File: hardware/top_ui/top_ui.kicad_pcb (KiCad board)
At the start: 2 copper layers, 52 x 52 mm, 26 parts, among them J1 USB-C, J2 J_STK_A, J3 J_STK_B, J5 ST77916 QSPI, J6 Stern, J7 Radar, Q1 BC847, Q2 P-FET 20V 1A, SW1A BTN1, SW1B BTN1, SW2A BTN2, SW2B BTN2, SW3A BTN3, SW3B BTN3, SW4A BTN4, SW4B BTN4, U1 USBLC6-2SC6, U2 SHT40-AD1B

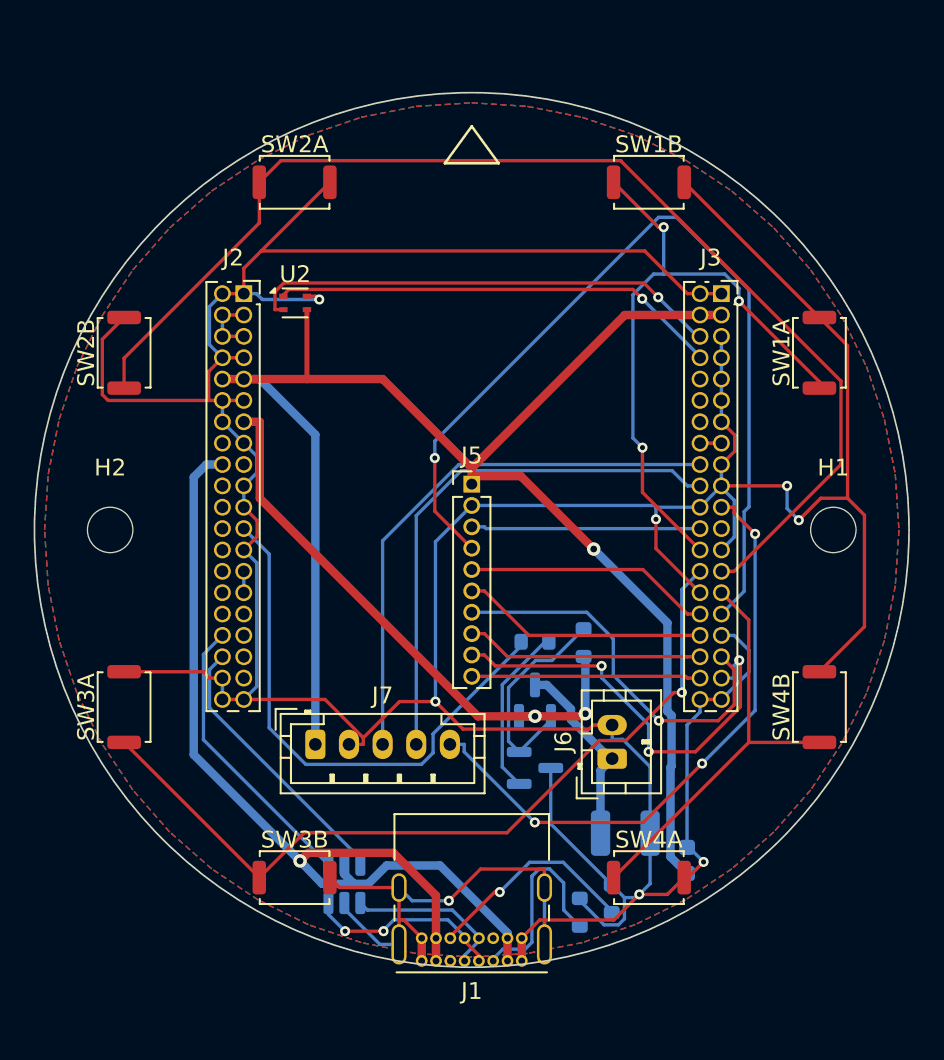
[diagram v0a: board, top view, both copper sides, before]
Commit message: Reed-Kontakte, Haubenkontakt, Klinkenbuchse, ToF statt Radar
Funktional neu
--------------
- Zwei Reed-Eingaenge fuer Fensterkontakte auf den einzigen noch freien
  Expanderpins P6/P7. 10k Pullup, 1k Serie, 100n und TVS je Kanal; bei
  geschlossenem Kontakt liegen 0,3 V am PCF8574, sicher unter VIL.
- Meldekontakt zur Dunstabzugshaube ueber PhotoMOS AQY282GS statt Relais:
  potentialfrei, 60 V / 0,8 A, kein Spulenstrom, keine Bauhoehe im 9-mm-
  Stapelspalt. NUR SELV - bei 230 V gehoert das Schaltglied nicht in die Dose.
- Weihnachtsstern jetzt gesteckt: Klinkenbuchse im oberen Steg der
  Frontplatte, PTC 0,2 A direkt an der Buchse gegen den Kurzschluss beim
  Stecken, Bulk vor die Sicherung gelegt.
- Radar durch VL53L1X (ToF) ersetzt. Hinter dieser Frontplatte hat kein
  20-mm-Radarmodul freie Sicht; der ToF passt als 4,9 x 2,5 mm grosser Chip
  in den Steg. Er misst Entfernung statt Empfindlichkeit - Schwelle exakt
  1 m - und deckt in der Fensterlaibung zugleich den Durchstieg ab.
  Netze umbenannt: RADAR_INT -> PRESENCE_INT, UART_RADAR_* -> UART_AUX_*.
  J7 bleibt unbestueckt als Reserve, damit das Stackpinout unberuehrt bleibt.

Frontplatte
-----------
Oberer Steg 9 -> 17 mm, damit Klinkenbuchse und ToF-Fenster nebeneinander
passen; Sicheln dadurch ~70 -> ~45 Grad, Stoesselwinkel 18 -> 12 Grad.
ToF-Kanal konisch (4,5 vorn, 3,0 hinten) fuer den Sichtkegel. Kabelausgang
Ø4,5 entfaellt. Selbsttests bestanden, STEP/STL neu erzeugt.

KiCad 10
--------
Die Generatoren liefen nur gegen KiCad-9-Bibliotheken. Migriert:
- Symbol- und Footprintpfad werden gefunden (Linux, macOS, Umgebungsvariable)
- PCF8574 -> PCF8574T (pinkompatibel, als Alias)
- Q_NMOS_GDS/Q_PMOS_GSD/Q_NPN_BCE liegen jetzt als hardware/lib/
  SwitchStack.kicad_sym im Projekt. KiCad 10 nummeriert die Stockvarianten
  mit G/D/S bzw. B/C/E - ein Alias haette die Anschluesse still vertauscht.
- USB-C-Schirm heisst SH statt S1, Zonen-API SetDoNotAllowZoneFills,
  DRC laeuft ueber kicad-cli statt WriteDRCRepo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
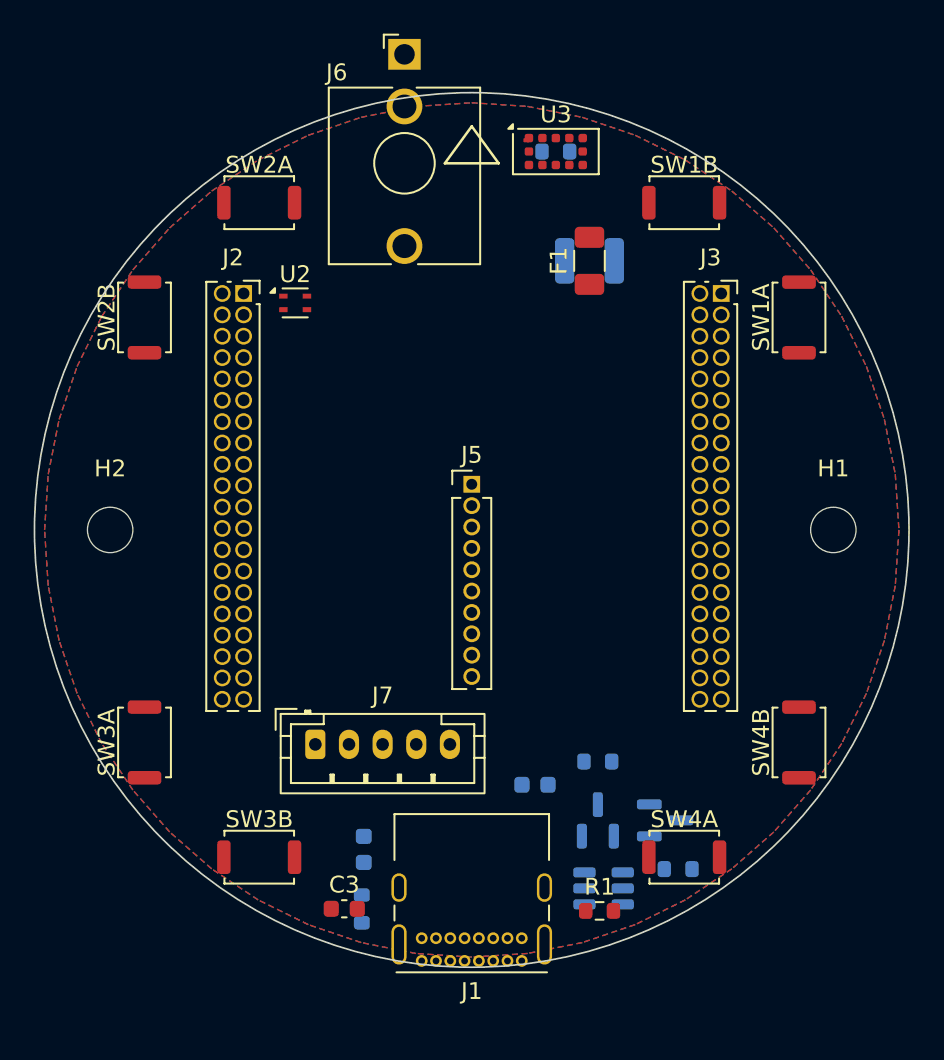
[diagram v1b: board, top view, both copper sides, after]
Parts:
- added C3: 100n, C_0603_1608Metric, F.Cu at (-7.58, 22.5)
- added C4: 4u7, C_0603_1608Metric, B.Cu at (-6.42, 19.0)
- added F1: 0,2 A PTC, Fuse_1206_3216Metric, F.Cu at (7.00, -16.0)
- added R5: 10k, R_0603_1608Metric, B.Cu at (5.00, -22.5)
- added U3: VL53L1X, ST_VL53L1x, F.Cu at (5.00, -22.5)
- J6: value Stern -> Stern Klinke; footprint JST_PH_B2B-PH-K_1x02_P2.00mm_Vertical -> Jack_3.5mm_QingPu_WQP-PJ398SM_Vertical_CircularHoles
- J7: value Radar -> Reserve UART
- R1: moved to F.Cu
- moved J6 43.7 mm to (-4.00, -28.3), turned to 0 degrees
- moved C2 34.1 mm to (7.00, -16.0)
- moved U1 15.4 mm to (7.84, 21.3), turned to 0 degrees
- moved R2 14.9 mm to (-6.54, 22.5)
- moved R4 14.6 mm to (12.3, 20.2), turned to 0 degrees
- moved Q2 10.5 mm to (11.5, 17.3), turned to 0 degrees
- moved C1 10.1 mm to (3.76, 15.2), turned to 0 degrees
- moved R3 8.04 mm to (7.50, 13.8)
- moved Q1 4.87 mm to (7.50, 17.3), turned to 90 degrees
- moved SW1A 2.43 mm to (19.5, -12.6)
- moved SW1B 2.43 mm to (12.6, -19.5)
- moved SW2A 2.43 mm to (-12.6, -19.5)
- moved SW2B 2.43 mm to (-19.5, -12.6)
- moved SW3A 2.43 mm to (-19.5, 12.6)
- moved SW3B 2.43 mm to (-12.6, 19.5)
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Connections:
- net RADAR_INT renamed PRESENCE_INT
- net UART_RADAR_RX renamed UART_AUX_RX
- net UART_RADAR_TX renamed UART_AUX_TX
- C2 pad 1: STAR_OUT -> STAR_SW
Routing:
- net PGND: track 302.5 -> 0.00 mm, vias 8 -> 0
- net 3V3_SYS: track 95.4 -> 0.00 mm, vias 1 -> 0
- net BTN2: track 70.8 -> 0.00 mm
- net USB_VBUS: track 58.7 -> 0.00 mm, vias 1 -> 0
- net QSPI_D0: track 53.2 -> 0.00 mm, vias 1 -> 0
- net BTN3: track 48.7 -> 0.00 mm, vias 1 -> 0
- net BTN1: track 38.8 -> 0.00 mm, vias 3 -> 0
- net PRESENCE_INT: track 36.4 -> 0.00 mm, vias 3 -> 0
- net 6V2_STAR_F: track 34.7 -> 0.00 mm, vias 2 -> 0
- net UART_AUX_TX: track 32.9 -> 0.00 mm
- net STAR_EN: track 32.2 -> 0.00 mm
- net UART_AUX_RX: track 32.0 -> 0.00 mm
- net I2C_SCL: track 28.4 -> 0.00 mm, vias 1 -> 0
- net I2C_SDA: track 26.7 -> 0.00 mm, vias 1 -> 0
- net DISP_RST: track 25.5 -> 0.00 mm, vias 3 -> 0
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
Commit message: Klinke nach 6 Uhr, ToF bleibt 12 Uhr - USB-C weicht nach oben aus
Beide Durchbrueche der Frontplatte sassen im oberen Steg. Der ToF gehoert
dorthin - er soll nach vorn und in die Fensteroeffnung schauen, nicht auf die
Fensterbank. Der Steckplatz gehoert nach unten, sonst haengt das Sternkabel
quer ueber der Anzeige.

Frontplatte
-----------
jack_x/jack_y von (-4,0 / +22,5) auf (0 / -22,5). Die Stegbreite bleibt: das
Ringskizze schneidet beide Rechtecke symmetrisch, alle vier Stege sind ohnehin
17 mm breit. Der Selbsttest pruefte fest verdrahtet den 90-Grad-Steg auf zwei
Durchbrueche; er sortiert die Loecher jetzt selbst nach Steg und prueft beide.
Materialbahnen: oben 11,25 und 1,25 mm, unten 5,70 und 5,70 mm. Selbsttest
BESTANDEN, STEP/STL neu erzeugt.

Top-Layout
----------
Die Klinke stand auf 6 Uhr im Weg - dort sass die USB-C-Buchse. Neue Ordnung:

  12 Uhr   ToF bei x=+5, USB-C links daneben (Mitte x=-3,875)
   6 Uhr   Klinkenbuchse mittig
   innen   J7 (Reserve-UART, DNP) nach rechts neben den Displayanschluss

Zur USB-C-Lage: Das Fenster zwischen dem ToF und dem Taster auf 123 Grad ist
knapp 12 mm breit. Tangential gedreht waechst die BBOX des Verbinders auf
12,2 mm - passt nicht. Achsparallel sind es 8,95 mm, es bleiben je 1,5 mm Luft.
Das Steckgesicht liegt dabei leicht innerhalb der Kontur; der Stecker ragt ueber
die 1 mm duenne Platine hinweg, das kostet nichts, waehrend Kupfer ueber der
Kante an die Dosenwand stiesse.

J7 musste weichen und findet automatisch keinen Platz: Als THT-Teil braucht er
beide Seiten frei, und die Vorderseite innerhalb r21 gehoert dem Displaymodul.
Deshalb wieder fest platziert, kurz zu J3, aus dem sein UART kommt.

Ergebnis: Platzierung kollisionsfrei, Randabstandsverletzungen 11 -> 1. Die
verbliebene ist der Platzhalter-Footprint der Klinke (Punkt 30): 14,4 mm lang
mit dem Bund in der Mitte, bei r = 22,5 steht das hintere Ende 3,3 mm ueber die
Kante. Punkt 30 nennt jetzt das Zielmass - das reale 2,5-mm-Teil muss in einen
Ring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
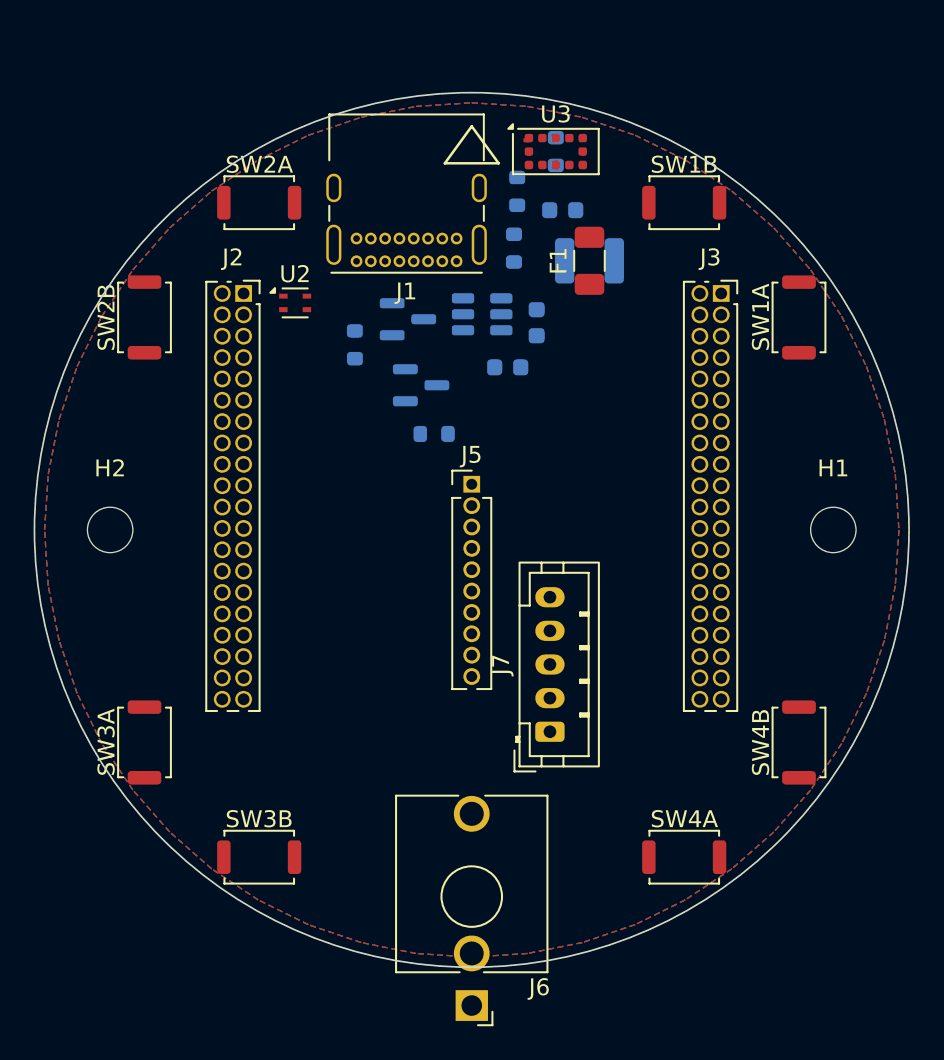
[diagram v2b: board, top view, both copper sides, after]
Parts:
- C3, R1: moved to B.Cu
- moved J6 56.7 mm to (0.00, 28.3), turned to 180 degrees
- moved R2 43.7 mm to (2.70, -20.1)
- moved J1 41.8 mm to (-0.90, -16.0)
- moved C4 39.8 mm to (5.41, -19.0), turned to 0 degrees
- moved R1 39.7 mm to (2.51, -16.8), turned to 90 degrees
- moved U1 34.9 mm to (0.62, -12.8)
- moved C3 33.6 mm to (2.14, -9.67)
- moved Q1 31.9 mm to (-3.79, -12.5), turned to 0 degrees
- moved Q2 29.7 mm to (-3.01, -8.60)
- moved R4 29.7 mm to (-2.24, -5.71)
- moved R3 28.7 mm to (-6.95, -11.0), turned to 90 degrees
- moved C1 27.5 mm to (3.86, -12.3), turned to 90 degrees
- moved J7 14.0 mm to (4.65, 12.0), turned to 90 degrees
- turned R5 to 90 degrees

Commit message: Weg A umgesetzt: Top-Board quadratisch, vier Ecktaster unter den Kreuzen
Umriss
------
gen_layouts.py und gen_boards.py kennen jetzt eine zweite Kontur. Das Top-Board
ist ein abgerundetes Quadrat, 49 x 49 mm mit Eckradius 4 - vier Geraden und vier
Boegen auf Edge.Cuts. Mid und Bottom bleiben rund und unangetastet; ihre
Boarddateien wurden nicht angefasst, die 985 Leiterbahnen des Bottom-Boards sind
unberuehrt.

Kantenmitte 24,5 liegt 0,5 mm innerhalb der Rastnasenlinie der Zentralscheibe
(50,0). Der Konturtest der Platzierung (inside_outline) rechnet die abgerundeten
Ecken korrekt mit, sonst haette die Automatik die Ecken verschenkt.

Taster
------
Acht parallelgeschaltete Sicheltaster werden vier Ecktaster, exakt auf
(+/-18,0 / +/-20,0) - den gemessenen Druckkreuzen der Scheibe. Ein Kreuz ist
3,2 mm gross und trifft genau einen Taster; parallelschalten waere sinnlos.
Der Schaltplan ist entsprechend neu erzeugt (25 statt 29 Bauteile,
Netzlistenvergleich bestanden), die Stuecklisten ebenfalls.

Durchbrueche
------------
Die vier Oeffnungen der Scheibe liegen jetzt bei (+/-9 / +/-19) - in den
Diagonalfeldern zwischen Pfeil und Ecktaster, mit rund 8 mm Abstand zu beiden.
Auf den Diagonalen selbst ist kein Platz mehr, dort sitzen die Kreuze. Links
oben ToF, links unten Klinke, rechts zweimal Lueftung - und weil dort die Luft
hereinkommt, sitzt der SHT4x jetzt unter dem oberen rechten Schlitz (Punkt 46).

Ergebnis: Platzierung kollisionsfrei, DRC unveraendert 28 clearance (die
bekannten Pad-Abstaende im USB-C-Footprint) plus die eine Randverletzung des
Klinken-Platzhalters.

Was dabei aufgefallen ist
-------------------------
gen_boards.py ueberschreibt hardware/<slug>/<slug>.kicad_pcb - es haette beim
naechsten Lauf die Bestueckung UND die Leiterbahnen aller drei Boards
weggeworfen. Das steht jetzt als Warnung im Docstring.

Der Fertigungsnutzen ist geloescht: gen_panel.py setzt drei Kreise Oe52
nebeneinander und wuerde um das quadratische Board eine runde Fraesbahn leg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
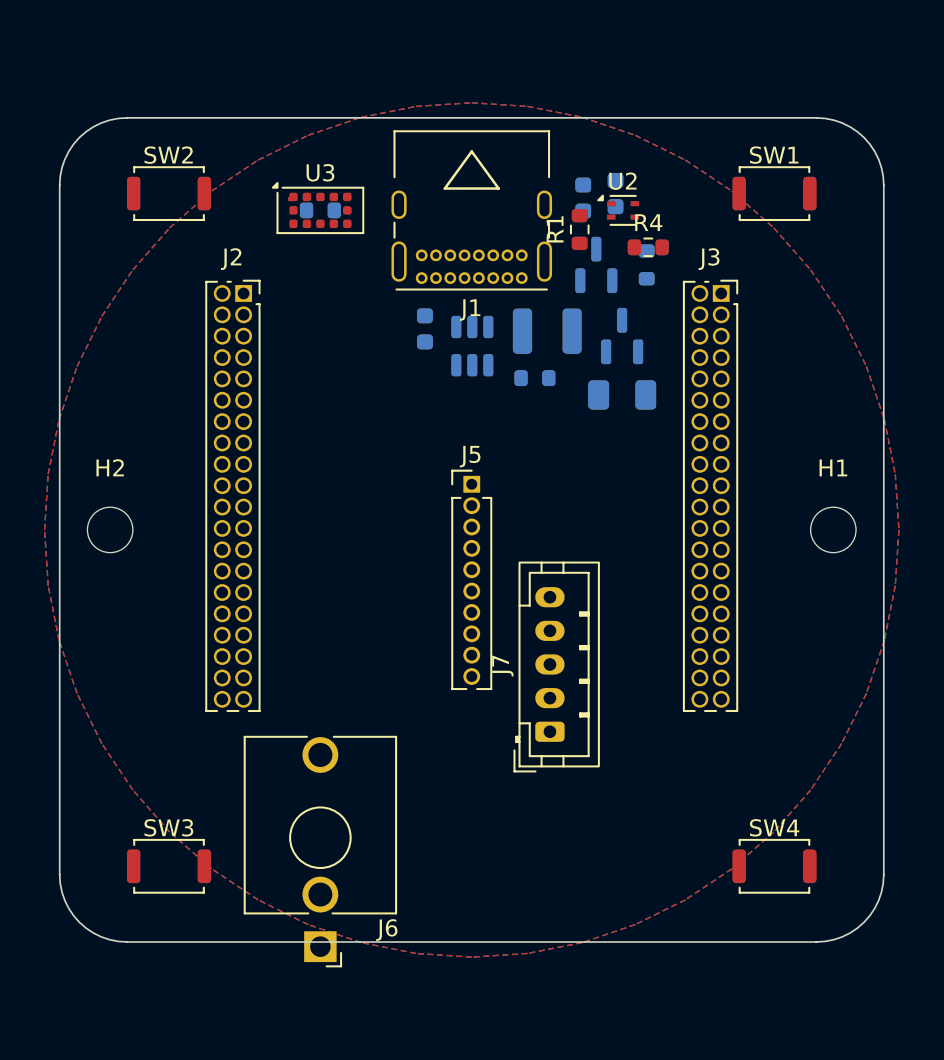
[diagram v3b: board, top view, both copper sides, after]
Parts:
- removed SW1A, SW1B: BTN1, SW_Push_SPST_NO_Alps_SKRK
- removed SW2A, SW2B: BTN2, SW_Push_SPST_NO_Alps_SKRK
- removed SW3A, SW3B: BTN3, SW_Push_SPST_NO_Alps_SKRK
- removed SW4A, SW4B: BTN4, SW_Push_SPST_NO_Alps_SKRK
- added SW1: BTN1, SW_Push_SPST_NO_Alps_SKRK, F.Cu at (18.0, -20.0)
- added SW2: BTN2, SW_Push_SPST_NO_Alps_SKRK, F.Cu at (-18.0, -20.0)
- added SW3: BTN3, SW_Push_SPST_NO_Alps_SKRK, F.Cu at (-18.0, 20.0)
- added SW4: BTN4, SW_Push_SPST_NO_Alps_SKRK, F.Cu at (18.0, 20.0)
- F1: moved to B.Cu
- R1, R4: moved to F.Cu
- moved U2 20.3 mm to (9.00, -19.0)
- moved R3 18.0 mm to (10.4, -15.8)
- moved R4 16.9 mm to (10.5, -16.8)
- moved R5 14.4 mm to (-9.00, -19.0), turned to 0 degrees
- moved U3 14.4 mm to (-9.00, -19.0)
- moved Q2 12.3 mm to (8.95, -11.5), turned to 90 degrees
- moved Q1 11.7 mm to (7.41, -15.8), turned to 90 degrees
- moved R2 11.2 mm to (3.76, -9.03), turned to 0 degrees
- moved J6 9.66 mm to (-9.00, 24.8)
- moved F1 8.21 mm to (8.95, -8.03), turned to 0 degrees
- moved C1 7.91 mm to (6.63, -19.7)
- moved C3 5.42 mm to (-2.78, -12.0), turned to 90 degrees
- moved C2 4.87 mm to (4.49, -11.8)
- moved R1 4.07 mm to (6.42, -17.9)
- moved J1 4.00 mm to (2.98, -15.0)
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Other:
- board size 52 x 52 mm -> 49 x 49 mm

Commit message: Adapter erzeugt; Top-Board auf 47 x 47 - die Tiefenkette gibt es vor
Beim Entwerfen des Adapters faellt die Groesse des Top-Boards als Rechnung an,
nicht als Wunsch. Die Tiefenkette von der Sichtflaeche nach hinten:

    0,0 .. 1,0   Zentralscheibe, Sichtflaeche
    1,0 .. 2,5   Druckkreuz auf ihrer Rueckseite
    2,5 .. 4,5   SMD-Taster ueber der Leiterplatte
    4,5 .. 5,5   Leiterplatte
           7,5   Rastebene und hinterer Rand der Scheibe

Die Rastebene liegt also HINTER der Platine. Der Schnapprand steht damit hinter
ihr und traegt sie zugleich - Rastglied und Auflage in einem. Und weil die
Scheibe auf lichte 50,0 rastet, der Rand aussen 49,8 misst und die Wand 1,4
braucht, bleiben innen genau 47,0. Nach unten begrenzen die Taster: Sie stehen
auf (+/-18 / +/-20), reichen mit Footprint bis 22,2, mit Randabstand also
mindestens 45,4. 47,0 liegt zwischen zwei harten Grenzen.

Board von 49 auf 47 geaendert, neu erzeugt, Platzierung weiter kollisionsfrei,
DRC unveraendert.

mechanical/adapter.py
---------------------
Neu, parametrisch, mit Selbsttest: Flansch 70 x 70 x 2,5 (darauf klemmen die
Doppelstege des Rahmens, F13), Schnapprand 49,8 mit zurueckspringendem Rastraum
fuer die vier Nasen, Platinentasche 47,4 mit 2,0 mm Auflage, zentrale
Durchfuehrung 43 x 43 fuer die Stackverbinder, Schraubschlitze auf 60 mm.
Gesamthoehe 10,0 mm. Der Selbsttest prueft die rechnerischen Bedingungen und
nimmt Materialproben an Rand, Rastraum, Auflage, Taschenwand und Schlitzen.

Geloescht: mechanical/frontplate.py samt Exporten und dem FreeCAD-Makro. Die
Sicheltasten waren eine vollstaendige Eigenentwicklung mit Kappen und
Stoesseln; mit der Zentralscheibe haben sie ihren Gegenstand verloren. Das
Modell liegt in der Git-Historie.

Co-Authored-By: Claude Opus 5 (1M context) <noreply@anthropic.com>
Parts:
- J5: value ST77916 QSPI -> ST7789 240x280
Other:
- board size 49 x 49 mm -> 47 x 47 mm
